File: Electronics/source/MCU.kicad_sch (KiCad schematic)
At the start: 64 parts, among them J1 Conn_01x05, J16 Conn_01x02, J2 Conn_01x03, J22 Conn_01x04, J3 Conn_01x03, J4 Conn_01x05, J6 Conn_01x20, J7 Conn_01x20, SW10 SW_Push, SW11 SW_Push, SW12 SW_Push, SW13 SW_Push, SW14 SW_Coded, SW4 SW_Push, SW5 SW_SPDT, SW6 SW_SPDT, SW7 SW_SPDT, SW8 SW_Push, SW9 SW_Push, U1 STM32F072CBTx, U4 LM2902, U5 ADP122AUJZ-3.3-R7, Y1 ABL-8.000MHZ-B2

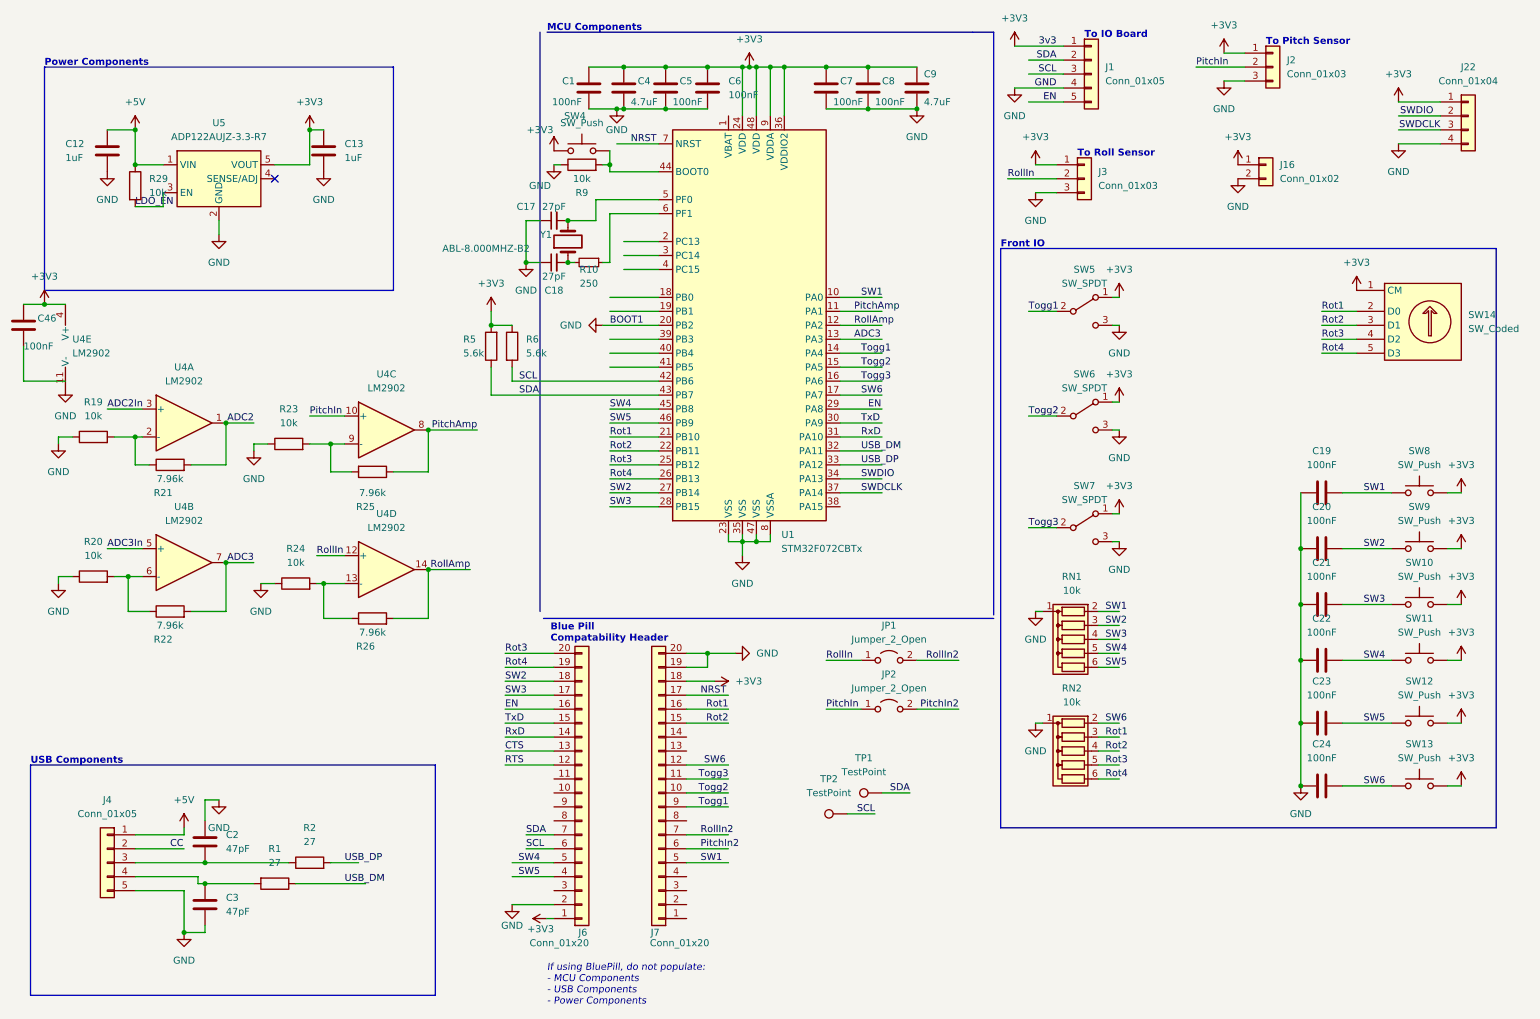
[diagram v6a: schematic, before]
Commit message: Added quick logo
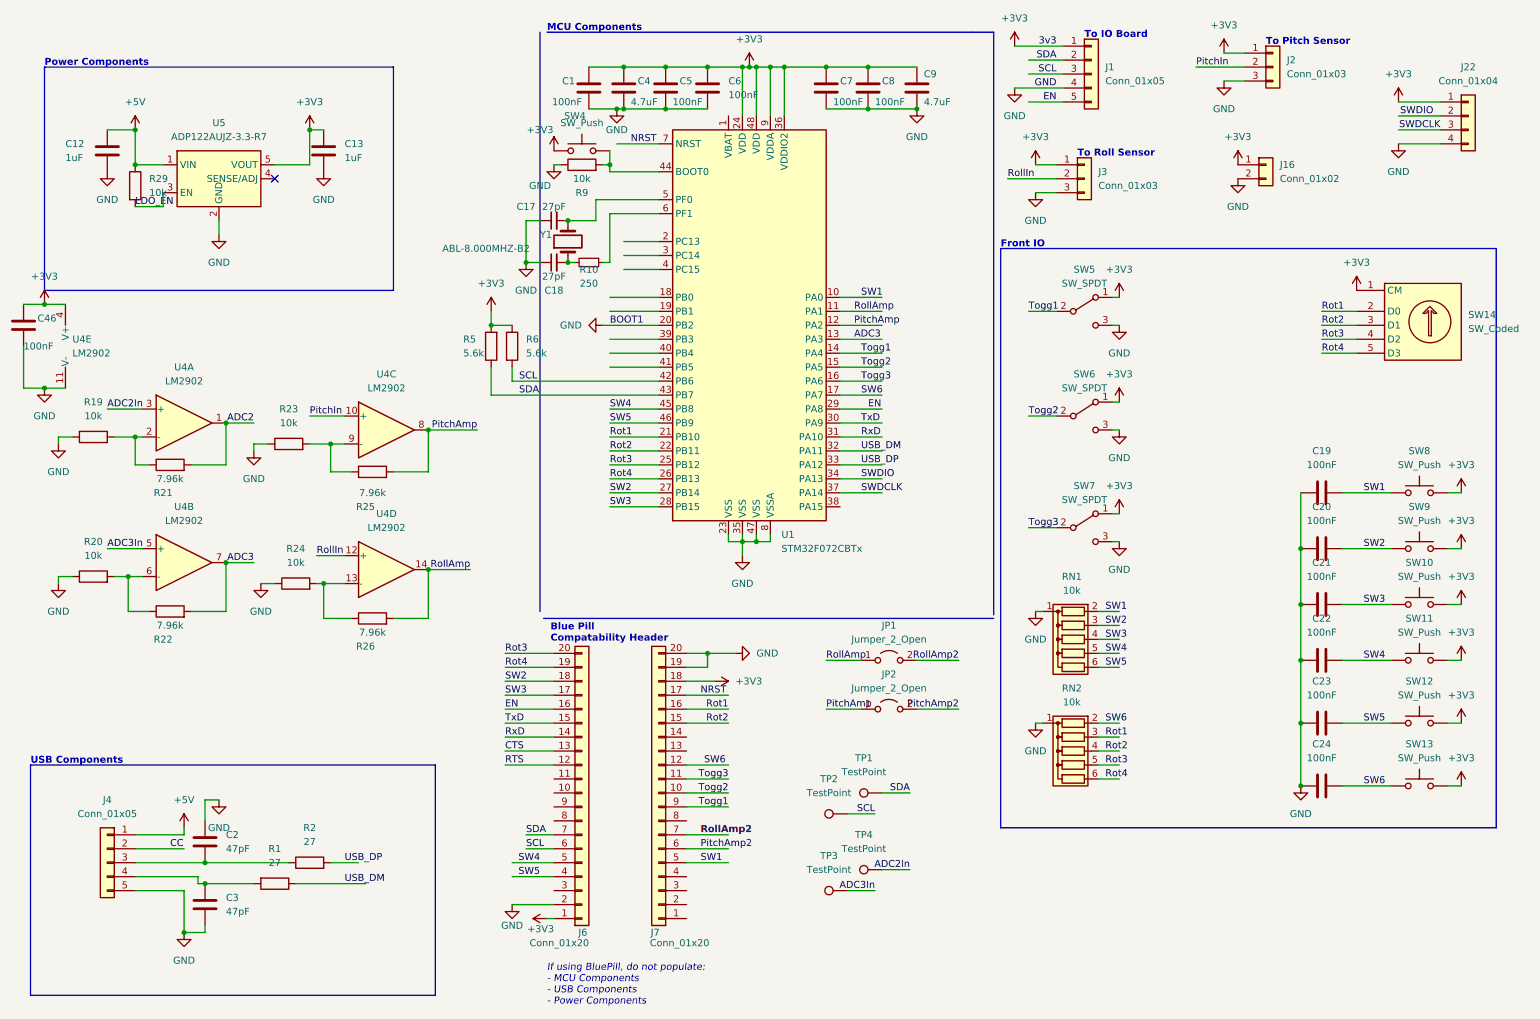
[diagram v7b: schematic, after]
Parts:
- added TP3, TP4: TestPoint, TestPoint:TestPoint_Pad_D1.0mm, symbol Connector:TestPoint
- C2, C3: now left out of the parts list
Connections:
- net ADC2In: now also TP4.1
- net ADC3In: now also TP3.1
- net GND: now also C46.2
- net PitchAmp: now also JP2.1 (A), U1.12 (PA2); no longer U1.11 (PA1)
- net PitchIn: no longer JP2.1 (A)
- net RollAmp: now also JP1.1 (A), U1.11 (PA1); no longer U1.12 (PA2)
- net RollIn: no longer JP1.1 (A)
- net PitchIn2 renamed PitchAmp2
- net RollIn2 renamed RollAmp2
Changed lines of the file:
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@@
   (junction (at 35.56 41.91) (diameter 0) (color 0 0 0 0)
+  )
+  (junction (at 19.05 82.55) (diameter 0) (color 0 0 0 0)
   )
   (junction (at 146.05 24.13) (diameter 0) (color 0 0 0 0)
@@
     (stroke (width 0) (type default) (color 0 0 0 0))
   )
-  (wire (pts (xy 15.24 74.93) (xy 15.24 81.28))
+  (wire (pts (xy 15.24 74.93) (xy 15.24 82.55))
     (stroke (width 0) (type default) (color 0 0 0 0))
   )
@@
     (stroke (width 0) (type default) (color 0 0 0 0))
   )
-  (wire (pts (xy 15.24 81.28) (xy 22.86 81.28))
+  (wire (pts (xy 15.24 82.55) (xy 19.05 82.55))
     (stroke (width 0) (type default) (color 0 0 0 0))
   )
@@
     (stroke (width 0) (type default) (color 0 0 0 0))
   )
+  (wire (pts (xy 171.45 170.18) (xy 176.53 170.18))
+    (stroke (width 0) (type default) (color 0 0 0 0))
+  )
   (wire (pts (xy 163.83 78.74) (xy 171.45 78.74))
     (stroke (width 0) (type default) (color 0 0 0 0))
@@
     (stroke (width 0) (type default) (color 0 0 0 0))
   )
+  (wire (pts (xy 19.05 82.55) (xy 22.86 82.55))
+    (stroke (width 0) (type default) (color 0 0 0 0))
+  )
   (wire (pts (xy 34.29 116.84) (xy 36.83 116.84))
     (stroke (width 0) (type default) (color 0 0 0 0))
@@
   )
   (wire (pts (xy 163.83 99.06) (xy 171.45 99.06))
+    (stroke (width 0) (type default) (color 0 0 0 0))
+  )
+  (wire (pts (xy 165.1 173.99) (xy 170.18 173.99))
     (stroke (width 0) (type default) (color 0 0 0 0))
   )
@@
     (effects (font (size 1.27 1.27)) (justify left bottom))
   )
-  (label "RollAmp" (at 166.37 71.12 0)
+  (label "PitchAmp" (at 166.37 71.12 0)
     (effects (font (size 1.27 1.27)) (justify left bottom))
   )
@@
     (effects (font (size 1.27 1.27)) (justify left bottom))
   )
-  (label "PitchIn2" (at 185.42 140.97 180)
+  (label "PitchAmp2" (at 185.42 140.97 180)
     (effects (font (size 1.27 1.27)) (justify right bottom))
   )
@@
     (effects (font (size 1.27 1.27)) (justify right bottom))
   )
-  (label "PitchIn2" (at 138.43 166.37 0)
+  (label "PitchAmp2" (at 138.43 166.37 0)
     (effects (font (size 1.27 1.27)) (justify left bottom))
   )
@@
     (effects (font (size 1.27 1.27)) (justify right bottom))
   )
-  (label "RollIn" (at 161.29 132.08 0)
+  (label "RollAmp" (at 161.29 132.08 0)
     (effects (font (size 1.27 1.27)) (justify left bottom))
   )
@@
     (effects (font (size 1.27 1.27)) (justify right bottom))
   )
-  (label "RollIn2" (at 138.43 163.83 0)
-    (effects (font (size 1.27 1.27)) (justify left bottom))
+  (label "RollAmp2" (at 138.43 163.83 0)
+    (effects (font (size 1.27 1.27) (thickness 0.254) bold) (justify left bottom))
   )
   (label "SW5" (at 109.22 171.45 180)
@@
     (effects (font (size 1.27 1.27)) (justify left bottom))
   )
-  (label "PitchAmp" (at 166.37 68.58 0)
+  (label "RollAmp" (at 166.37 68.58 0)
     (effects (font (size 1.27 1.27)) (justify left bottom))
   )
@@
     (effects (font (size 1.27 1.27)) (justify left bottom))
   )
-  (label "RollIn2" (at 185.42 132.08 180)
+  (label "RollAmp2" (at 185.42 132.08 180)
     (effects (font (size 1.27 1.27)) (justify right bottom))
   )
@@
     (effects (font (size 1.27 1.27)) (justify left bottom))
   )
+  (label "ADC3In" (at 170.18 173.99 180)
+    (effects (font (size 1.27 1.27)) (justify right bottom))
+  )
   (label "Rot3" (at 102.87 130.81 0)
     (effects (font (size 1.27 1.27)) (justify left bottom))
@@
     (effects (font (size 1.27 1.27)) (justify left bottom))
   )
+  (label "ADC2In" (at 176.53 170.18 180)
+    (effects (font (size 1.27 1.27)) (justify right bottom))
+  )
   (label "SW2" (at 212.09 125.73 0)
     (effects (font (size 1.27 1.27)) (justify left bottom))
@@
     (effects (font (size 1.27 1.27)) (justify left bottom))
   )
-  (label "PitchIn" (at 161.29 140.97 0)
+  (label "PitchAmp" (at 161.29 140.97 0)
     (effects (font (size 1.27 1.27)) (justify left bottom))
   )
@@
   )
   (symbol (lib_id "Device:C") (at 48.26 165.1 180) (unit 1)
-    (in_bom yes) (on_board yes) (fields_autoplaced)
+    (in_bom no) (on_board yes) (fields_autoplaced)
     (property "Reference" "C2" (id 0) (at 52.07 163.8299 0)
       (effects (font (size 1.27 1.27)) (justify right))
@@
   )
   (symbol (lib_id "Device:C") (at 48.26 176.53 0) (unit 1)
-    (in_bom yes) (on_board yes) (fields_autoplaced)
+    (in_bom no) (on_board yes) (fields_autoplaced)
     (property "Reference" "C3" (id 0) (at 52.07 175.2599 0)
       (effects (font (size 1.27 1.27)) (justify left))
@@
     (pin "1")
   )
+  (symbol (lib_id "Connector:TestPoint") (at 171.45 170.18 90) (unit 1)
+    (in_bom yes) (on_board yes) (fields_autoplaced)
+    (property "Reference" "TP4" (id 0) (at 168.148 163.83 90))
+    (property "Value" "TestPoint" (id 1) (at 168.148 166.37 90))
+    (property "Footprint" "TestPoint:TestPoint_Pad_D1.0mm" (id 2) (at 171.45 165.1 0)
+      (effects (font (size 1.27 1.27)) hide)
+    )
+    (property "Datasheet" "~" (id 3) (at 171.45 165.1 0)
+      (effects (font (size 1.27 1.27)) hide)
+    )
+    (pin "1")
+  )
   (symbol (lib_id "Switch:SW_Push") (at 269.24 143.51 0) (unit 1)
     (in_bom yes) (on_board yes) (fields_autoplaced)
@@
     (pin "1")
   )
-  (symbol (lib_id "power:GND") (at 22.86 82.55 0) (unit 1)
-    (in_bom yes) (on_board yes) (fields_autoplaced)
-    (property "Reference" "#PWR0212" (id 0) (at 22.86 88.9 0)
-      (effects (font (size 1.27 1.27)) hide)
-    )
-    (property "Value" "GND" (id 1) (at 22.86 87.63 0))
-    (property "Footprint" "" (id 2) (at 22.86 82.55 0)
-      (effects (font (size 1.27 1.27)) hide)
-    )
-    (property "Datasheet" "" (id 3) (at 22.86 82.55 0)
+  (symbol (lib_id "power:GND") (at 19.05 82.55 0) (unit 1)
+    (in_bom yes) (on_board yes) (fields_autoplaced)
+    (property "Reference" "#PWR0212" (id 0) (at 19.05 88.9 0)
+      (effects (font (size 1.27 1.27)) hide)
+    )
+    (property "Value" "GND" (id 1) (at 19.05 87.63 0))
+    (property "Footprint" "" (id 2) (at 19.05 82.55 0)
+      (effects (font (size 1.27 1.27)) hide)
+    )
+    (property "Datasheet" "" (id 3) (at 19.05 82.55 0)
       (effects (font (size 1.27 1.27)) hide)
     )
@@
     (pin "2")
   )
+  (symbol (lib_id "Connector:TestPoint") (at 165.1 173.99 90) (unit 1)
+    (in_bom yes) (on_board yes) (fields_autoplaced)
+    (property "Reference" "TP3" (id 0) (at 161.798 167.64 90))
+    (property "Value" "TestPoint" (id 1) (at 161.798 170.18 90))
+    (property "Footprint" "TestPoint:TestPoint_Pad_D1.0mm" (id 2) (at 165.1 168.91 0)
+      (effects (font (size 1.27 1.27)) hide)
+    )
+    (property "Datasheet" "~" (id 3) (at 165.1 168.91 0)
+      (effects (font (size 1.27 1.27)) hide)
+    )
+    (pin "1")
+  )
   (symbol (lib_id "power:GND") (at 21.59 118.11 0) (unit 1)

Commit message: corrected incomplete USB for flipable cable, and replaced termination resistors w jumpers
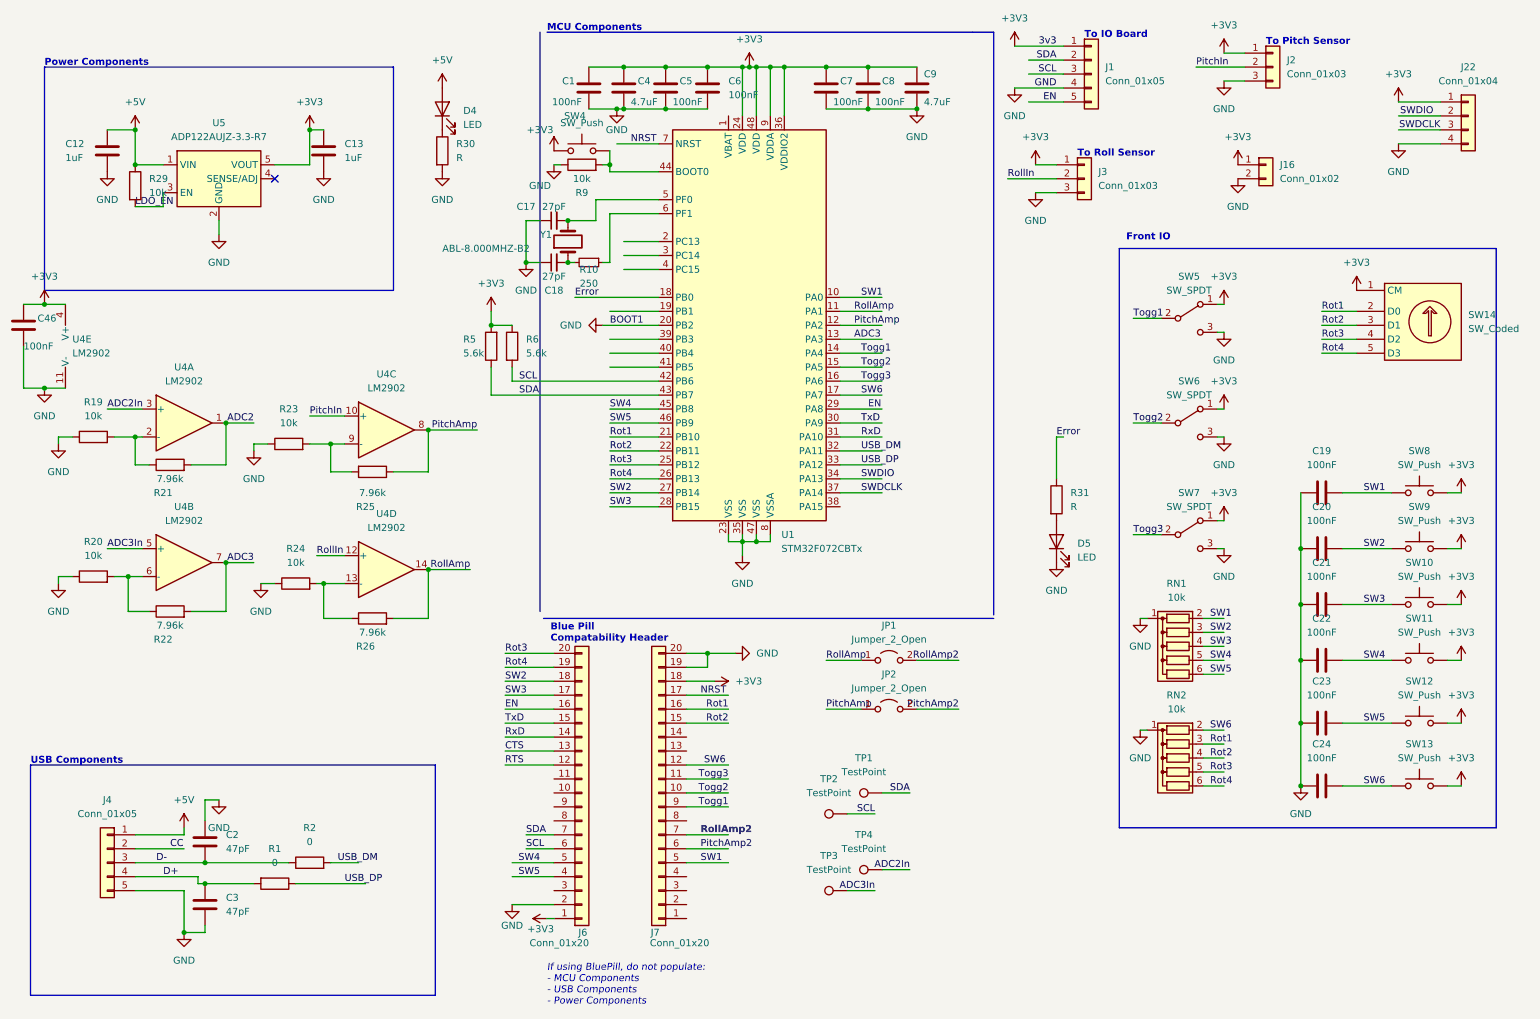
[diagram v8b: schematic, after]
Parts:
- added D4, D5: LED, LED_SMD:LED_0603_1608Metric_Pad1.05x0.95mm_HandSolder, symbol Device:LED
- added R30: R, Resistor_SMD:R_0805_2012Metric, symbol Device:R
- added R31: R, Resistor_SMD:R_0805_2012Metric_Pad1.20x1.40mm_HandSolder, symbol Device:R
- R1, R2: value 27 -> 0
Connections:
- net +5V: now also D4.2 (A)
- net GND: now also D5.1 (K), R30.2
- net USB_DM: now also R2.2; no longer R1.1
- net USB_DP: now also R1.1; no longer R2.2
- net Error: now reaches U1.18 (PB0)
- net Error: now also R31.1
- net  D-: now reaches C2.1, J4.3 (Pin_3), R2.1
- net D+: now reaches C3.1, J4.4 (Pin_4), R1.2
- new net: D4.1 (K), R30.1
- new net: D5.2 (A), R31.2
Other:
- moved on the sheet: RN1, RN2, SW5, SW6, SW7
